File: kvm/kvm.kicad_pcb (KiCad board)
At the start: 4 copper layers, 56.4 x 69.3 mm, 61 parts, among them J1 USB4110-GF-A, J2 USB4110-GF-A, J3 USB_A_Stacked, J4 USB_A_Stacked, Q1 Q_PMOS_GSD, SW1 SW_DPDT_x2, U1 SRV05-4, U2 LTC4412xS6, U3 FSUSB42MUX, U4 GL850G, U5 SRV05-4, U6 SRV05-4, Y1 Crystal

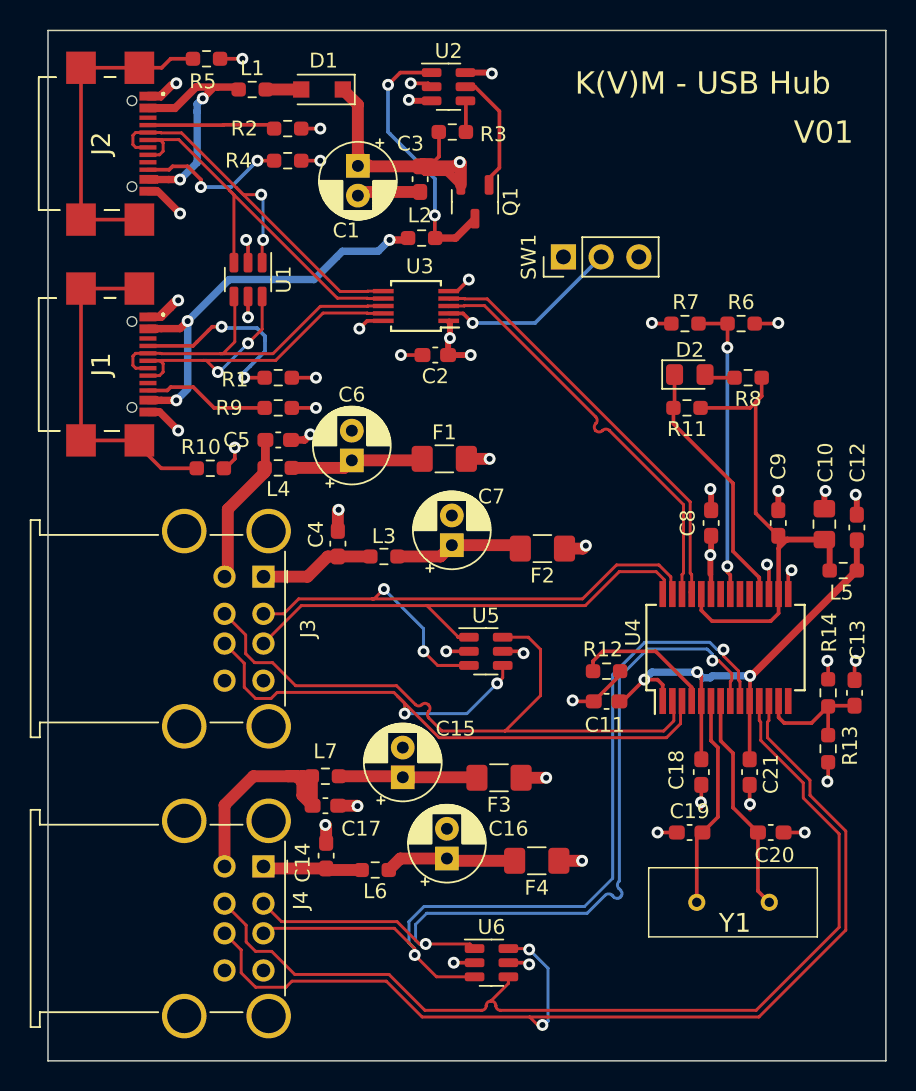
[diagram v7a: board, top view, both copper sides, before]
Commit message: updated layout
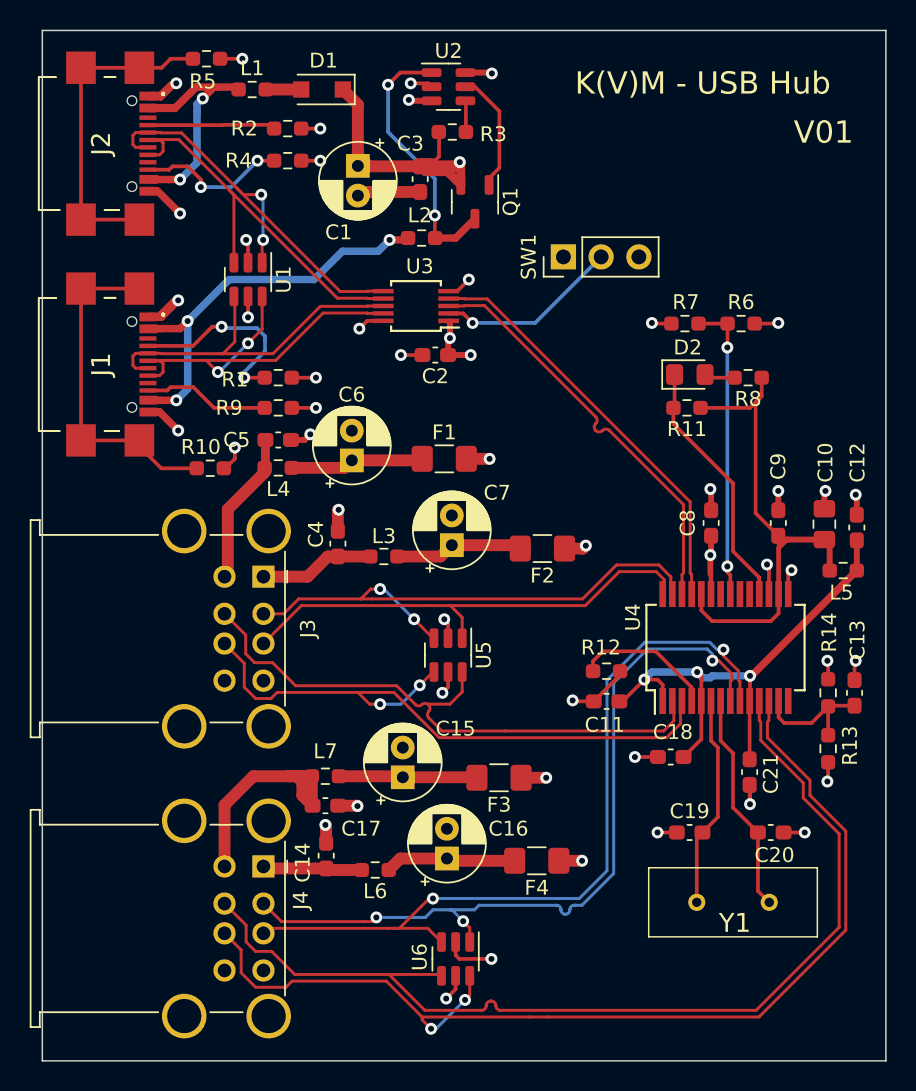
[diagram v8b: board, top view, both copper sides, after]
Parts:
- moved U5 2.55 mm to (87.2, 81.4), turned to -90 degrees
- moved U6 2.43 mm to (87.8, 101.9), turned to -90 degrees
- moved C18 2.29 mm to (102.2, 88.3), turned to 180 degrees
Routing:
- net D3+: track 59.5 -> 53.9 mm
- net D2-: track 45.9 -> 40.5 mm
- net D1-: track 42.0 -> 36.9 mm
- net D3-: track 58.1 -> 53.4 mm, vias 2 -> 3
- net GND: track 69.0 -> 72.4 mm
- net D2+: track 46.4 -> 42.9 mm
- net D4+: track 73.8 -> 71.3 mm
- net D1+: track 35.1 -> 32.7 mm
- net D4-: track 67.5 -> 69.2 mm
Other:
- board size 56.4 x 69.3 mm -> 56.8 x 69.3 mm
